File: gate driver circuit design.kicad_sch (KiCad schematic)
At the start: 22 parts, among them U1 SN6501QDBVRQ1, U2 SN6501QDBVRQ1

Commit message: Completed schematic design of gate driver
added components to schematic 27th May 2024
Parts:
- removed U2: SN6501QDBVRQ1, SOT95P280X145-5N, symbol SN6501QDBVRQ1:SN6501QDBVRQ1
- added C16, C18, C23, C26, C7: 4.7µF, symbol Device:C
- added C17, C19, C23, C24 (x2), C25, C27, C33, C37: 0.1µF, symbol Device:C
- added C20, C21, C25, C28: 0.01µF, symbol Device:C
- added C22, C35, C41, C42, C43: 100µF, symbol Device:C
- added C29: 100pF, symbol Device:C
- added C34: 27pF, symbol Device:C
- added C36: 470pF, symbol Device:C
- added C39, C40: 1000pF, symbol Device:C
- added D1, D2: BAV70-E3-08, SOT_70-E3-08_VIS, symbol 2024-05-25_06-21-47:BAV70-E3-08
- added D3, D4: MBRA340T3G, DIOM5226X220N, symbol MBRA340T3G:MBRA340T3G
- added D4, Q2, Q3: MMBT3904T-7-F, SOT50P160X90-3N, symbol MMBT3904T-7-F:MMBT3904T-7-F
- added D5, D7, D8: 1N4148X-TP, SODFL1608X70N, symbol 1N4148X-TP:1N4148X-TP
- added D6: BYG23T-M3/TR, DIOM5127X229N, symbol BYG23T-M3_TR:BYG23T-M3_TR
- added D9: 5.1V, SOD3716X135N, symbol BZT52C5V1-G3-08:BZT52C5V1-G3-08
- added IC1: LMV762QMA_NOPB, SOIC127P600X175-8N, symbol LMV762QMA_NOPB:LMV762QMA_NOPB
- added J101: 90122-0763, 90122-0763:MOLEX_90122-0763, symbol 90122-0763:90122-0763
- added J102, J103: 90121-0762, HDRRA2W64P0X254_1X2_508X250X360P, symbol 90121-0762:90121-0762
- added Q1: CSD17313Q2, CSD17313Q2:TRANS_CSD17313Q2, symbol CSD17313Q2:CSD17313Q2
- added R10, R7: 5.11, symbol Device:R
- added R11, R8: 1.0, symbol Device:R
- added R12, R14, R18, R28: 10.0k, symbol Device:R
- added R13, R22: 2.2k, symbol Device:R
- added R13: 27, symbol Device:R
- added R132, R27: 0, symbol Device:R
- added R15, R20, R23, R25, R26, R30: 5.1k, symbol Device:R
- added R16, R17, R19: 1.0k, symbol Device:R
- added R21: 1.00k, symbol Device:R
- added R24: 2k, symbol Device:R
- added R29: 15k, symbol Device:R
- added R8, R9 (x2): R, symbol Device:R
- added T1, T2: 750343725, PushPull_750343725:WE-PPTI_1209_L12.7W9.14H7.62, symbol PushPull_750343725:750343725
- added U2: TPS7B6950QDCYRQ1, TPS7B6950QDCYRQ1:VREG_TPS7B6950QDCYRQ1, symbol TPS7B6950QDCYRQ1:TPS7B6950QDCYRQ1
- added U3, U5, U9: TL431AQDBZRQ1, DBZ3, symbol TL431AQDBZRQ1:TL431AQDBZRQ1
- added U4: SN6501QDBVRQ1, SOT95P280X145-5N, symbol SN6501QDBVRQ1:SN6501QDBVRQ1
- added U6: UCC21530QDWKRQ1, UCC21530QDWKRQ1, symbol UCC21530QDWKRQ1:UCC21530QDWKRQ1
- added U7: ISO7721QDRQ1, SOIC127P600X175-8N, symbol ISO7721QDRQ1:ISO7721QDRQ1
- C15: value 0.1µF -> C
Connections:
- net 5Vin is gone; now on net GND: C10.1, C11.1, C2.1, C3.1, U1.2 (VCC)
- net +15Va: now also C19.1, C20.1, D1.3; no longer C12.2, C13.2, C14.2, C9.2, R4.1
- net -4Va: now also C16.1, C17.1, C21.1, T1.5, T2.5, U3.3 (ANODE), U5.3 (ANODE), U6.14 (VSSA); no longer C1.1, C15.2, C8.2, C9.1, R1.2, R2.1, R4.2, R5.1
- net GND: now also C22.1, C22.2, C35.1, D4.2 (E), J101.3, R132.2, R30.1, T1.2, T2.2, U4.2 (VCC), U4.4 (GND_1), U4.5 (GND_2), U6.3 (VCCI_1), U6.8 (VCCI_2), U7.1 (VCC1), U7.4 (GND1)
- net at R2.2, R3.1: now also U3.2 (REF)
- net at R5.2, R6.1: now also U5.2 (REF)
- net at U1.1 (D1): now also T1.3
- net at U1.3 (D2): now also T1.1
- new net: D2.1, T2.6
- new net: D2.2, T2.4
- new net: C41.2, R9.2, U6.2 (INB)
- new net: C41.1, C42.1, C43.1, R9.2, U6.4 (GND)
- new net: C43.2, R9.1, U6.6 (DT)
- new net: C42.2, R8.2, U6.1 (INA)
- new net: C24.2, D4.1 (K), R10.1, U6.10 (OUTB)
- new net: C23.2, D3.1 (K), R7.1, U6.15 (OUTA)
- new net: C18.1, U6.16 (VDDA)
- new net: D4.3 (C), R27.1, R30.2, U6.5 (EN)
- new net: IC1.3 (+IN_A), Q3.3 (C), R17.2, R21.1
- new net: C35.2, R23.2, U7.3 (INB)
- new net: C34.2, D8.1 (K), R21.2, R25.2
- new net: D7.2 (A), IC1.1 (OUT_A), R16.1, R22.2
- new net: Q2.1 (B), R16.2
- new net: D3.2 (A), R8.1
- new net: T2.3, U4.1 (D1)
- new net: T2.1, U4.3 (D2)
- new net: IC1.2 (-IN_A), IC1.6 (-IN_B), R20.1, R24.2, U9.1 (CATHODE)
- new net: IC1.5 (+IN_B), R22.1
- new net: IC1.7 (OUT_B), U7.7 (INA)
- new net: D7.1 (K), R17.1
- new net: Q1.3, Q2.2 (E), R19.1
- new net: D8.2 (A), D9.1 (K), R18.1, R26.2
- new net: D1.1, T1.6
- new net: D1.2, T1.4
- new net: Q1.1, Q1.2, Q1.5, Q1.6, Q1.8, R13.1
- new net: D5.2 (A), D6.2 (A), R15.1, R18.2
- new net: J101.4, R132.1
- new net: R24.1, R28.2, U9.2 (REF)
- new net: D4.2 (A), R11.1
- new net: C25.1, R13.2
- new net +15Vb: C12.2, C13.2, C14.2, C26.1, C27.1, C28.1, C9.2, D2.3, R4.1, U2.1 (IN), U6.11 (VDDB)
- new net -4Vb: C23.1, C24.1, C25.1, C29.1, C33.1, C34.1, C36.1, C37.1, C7.2, D9.2 (A), IC1.4 (V-), Q1.4, Q1.7, Q3.2 (E), R13.1, R19.2, R25.1, R26.1, R28.1, R29.1, U2.2 (GND_2), U2.4 (GND_4), U6.9 (VSSB), U7.5 (GND2), U7.6 (OUTB), U9.3 (ANODE)
- new net Coma: C1.1, C16.2, C17.2, C18.2, C19.2, C20.2, C21.2, C39.1, C8.2, D6.1 (K), J103.1, R1.2, R12.2, R2.1, U3.1 (CATHODE)
- new net Comb: C15.2, C23.2, C24.2, C25.2, C26.2, C27.2, C28.2, C40.1, C9.1, J102.1, R14.2, R4.2, R5.1, U5.1 (CATHODE)
- new net FLT: D4.1 (B), J101.2, R27.2, U7.2 (OUTA)
- new net G1: C23.1, C39.2, J103.2, R12.1, R7.2, R8.2
- new net G2: C24.1, C25.2, C40.2, D5.1 (K), J102.2, R10.2, R11.2, R14.1, R15.2
- new net RESET: J101.1, R23.1
- new net Vcc5V: C29.2, C33.2, C37.2, C7.1, IC1.8 (V+), Q2.3 (C), Q3.1 (B), R13.2, R20.2, R29.2, U2.3 (OUT), U7.8 (VCC2)
- new net Vg1: J101.6, R8.1
- new net Vg2: J101.5, R9.1
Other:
- note added: "750343725"
- note added: "Bottom Switch"
- note added: "Top Switch"
- moved on the sheet: C1, C2, C3, C4, C5, C6, C8, R1, R2, R3, U1

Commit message: Schematic Design Completed For Gate Driver
Schematic Design Completed For Gate Driver
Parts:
- removed C1, C11, C14, C17, C19, C23, C24 (x2), C25, C27, C3, C33, C37, C6, C9: 0.1µF, symbol Device:C
- removed C10, C2: 10µF, symbol Device:C
- removed C12, C13, C16, C18, C23, C26, C4, C5, C7: 4.7µF, symbol Device:C
- removed C15, C8: C, symbol Device:C
- removed C20, C21, C25, C28: 0.01µF, symbol Device:C
- removed C22, C35, C41, C42, C43: 100µF, symbol Device:C
- removed C29: 100pF, symbol Device:C
- removed C34: 27pF, symbol Device:C
- removed C36: 470pF, symbol Device:C
- removed C39, C40: 1000pF, symbol Device:C
- removed R1, R4: 4.7k, symbol Device:R
- removed R10, R7: 5.11, symbol Device:R
- removed R11, R8: 1.0, symbol Device:R
- removed R12, R14, R18, R28: 10.0k, symbol Device:R
- removed R13, R22: 2.2k, symbol Device:R
- removed R13: 27, symbol Device:R
- removed R132: 0, symbol Device:R
- removed R15, R20, R23, R25, R26, R30: 5.1k, symbol Device:R
- removed R16, R17, R19: 1.0k, symbol Device:R
- removed R2, R5: 3.01k, symbol Device:R
- removed R21: 1.00k, symbol Device:R
- removed R24: 2k, symbol Device:R
- removed R29: 15k, symbol Device:R
- removed R3, R6: 4.99k, symbol Device:R
- removed R8, R9 (x2): R, symbol Device:R
- added C1, C11, C14, C15, C17, C19, C22, C25, C27, C29, C3, C32, C33, C37, C6, C8, C9: 0.1µF, CAPC2012X90N, symbol 0805B104K250CT:0805B104K250CT
- added C10, C2: 10µF, CAPC2012X135N, symbol LMK212ABJ106KGHT:LMK212ABJ106KGHT
- added C12, C13, C16, C18, C26, C28, C4, C5, C7: 4.7µF, GRT21BR61E226ME13L, symbol GRT21BR61H475KE13L:GRT21BR61H475KE13L
- added C20, C21, C30, C31: 0.01µF, CAPC2012X95N, symbol GRM2195C1H103JA01D:GRM2195C1H103JA01D
- added C23, C24: 0.1µF, CAPC2012X95N, symbol AC0805KRX7R8BB104:AC0805KRX7R8BB104
- added C34: 27pF, CAPC2012X70N, symbol CC0805JRNPO9BN270:CC0805JRNPO9BN270
- added C35: 100µF, CAPC2012X75N, symbol CL21C101JBANNNC:CL21C101JBANNNC
- added C36: 470pF, C0805, symbol C0805C471J5GACTU:C0805C471J5GACTU
- added C38, C41, C42, C43: 100pF, C0805, symbol C0805C101J1GACAUTO:C0805C101J1GACAUTO
- added C39, C40: 1000pF, C0805, symbol C0805C102K5RACAUTO:C0805C102K5RACAUTO
- added R1, R4: 4.7k, RESC2012X50N, symbol CRCW08054K70JNEA:CRCW08054K70JNEA
- added R10, R7: 5.11, RESC3216X60N, symbol CRCW12065R11FKEA:CRCW12065R11FKEA
- added R11, R8: 1.0, RESC3116X65N, symbol CRM1206-JW-1R0ELF:CRM1206-JW-1R0ELF
- added R12, R14, R18, R28: 10.0k, RESC2012X60N, symbol RC0805JR-131KL:RC0805JR-131KL
- added R13: 27, RESC3216X60N, symbol CRCW120627R0JNEA:CRCW120627R0JNEA
- added R132, R33, R34: 0, ERJS06_U06_(0805), symbol ERJ-U060R00V:ERJ-U060R00V
- added R15, R20, R23, R25, R26, R30, R32: 5.1k, RESC2012X60N, symbol CR0805-FX-5101ELF:CR0805-FX-5101ELF
- added R16, R17, R19, R27: 1.0k, RESC2012X60N, symbol RC0805JR-131KL:RC0805JR-131KL
- added R2, R5: 3.01k, RESC2012X60N, symbol RC0805JR-131KL:RC0805JR-131KL
- added R21: 1.00k, RESC2012X60N, symbol RC0805JR-131KL:RC0805JR-131KL
- added R22: 2.2k, RESC2012X60N, symbol RC0805JR-131KL:RC0805JR-131KL
- added R24: 2.00k, RESC2012X60N, symbol RC0805JR-131KL:RC0805JR-131KL
- added R29: 15k, RESC2012X50N, symbol CRCW080515K0JNEA:CRCW080515K0JNEA
- added R3, R6: 4.99k, RESC2013X65N, symbol RR1220P-4991-D-M:RR1220P-4991-D-M
- added R9: 1k, RESC2012X60N, symbol RC0805JR-131KL:RC0805JR-131KL
- renumbered D4 to Q4, R27 to R31, IC1 to U8
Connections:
- net +15Va: now also C1.2, C19.1, C20.1, C4.2, C5.2, C6.2, R1.2
- net +15Vb: now also C12.2, C13.2, C14.2, C28.2, C29.2, C31.2, C9.2, R4.2
- net -4Va: now also C16.1, C17.1, C21.1, C4.1, C5.1, C6.1, C8.1, R3.1 (R1); no longer T2.5, U5.3 (ANODE)
- net -4Vb: now also T2.5, U5.3 (ANODE), C12.1, C13.1, C14.1, C15.1, C26.2, C27.2, C30.2, C33.1, C34.1, C36.1, C36.2, C37.1, C38.1, C7.1, R19.2, R25.1, R26.1, R27.1, R28.1, R29.1, R6.1 (R1)
- net Coma: now also C1.1, C16.2, C17.2, C18.2, C19.2, C20.2, C21.2, C39.2, C8.2, R1.1, R12.1, R2.2
- net Comb: now also C15.2, C26.1, C27.1, C28.1, C29.1, C30.1, C31.1, C40.2, C9.1, R14.1, R4.1, R5.2
- net FLT: now also R32.2; no longer Q4.1 (B)
- net G1: now also C23.2, C39.1, R12.2, R7.2, R8.2
- net G2: now also C24.2, C25.2, C40.1, R10.2, R11.2, R14.2, R15.2
- net GND: now also C10.2, C11.1, C2.2, C22.1, C3.1, C32.1, C35.1; no longer T1.2, T2.2, U1.2 (VCC), U4.2 (VCC), U6.3 (VCCI_1), U6.8 (VCCI_2), U7.1 (VCC1)
- net RESET: now also R23.2
- net Vcc5V: now also C33.2, C37.2, C38.2, C7.2, R20.2, R27.2, R29.2
- net Vg1: now also R33.1
- net Vg2: now also R34.1
- net at U6.2 (INB): now also C41.2, R34.2
- net at U6.4 (GND): now also C41.1, C42.1, C43.1, R9.1
- net at U6.6 (DT): now also C43.2, R9.2
- net at U6.1 (INA): now also C42.2, R33.2
- net at D4.1 (K), U6.10 (OUTB): now also C24.1, R10.1
- net at D3.1 (K), U6.15 (OUTA): now also C23.1, R7.1
- net at U6.16 (VDDA): now also C18.1
- net at Q4.3 (C), R31.1, U6.5 (EN): now also R30.1
- net at Q3.3 (C), U8.3 (+IN_A): now also R17.2, R21.2
- net at U7.3 (INB): now also C35.2, R23.1
- net at U3.2 (REF): now also R2.1, R3.2 (R2)
- net at U5.2 (REF): now also R5.1, R6.2 (R2)
- net at D8.1 (K): now also C34.2, R21.1, R25.2
- net at D7.2 (A), U8.1 (OUT_A): now also R16.1, R22.1
- net at Q2.1 (B): now also R16.2
- net at D3.2 (A): now also R8.1
- net at U8.2 (-IN_A), U8.6 (-IN_B), U9.1 (CATHODE): now also R20.1, R24.2
- net at U8.5 (+IN_B): now also R22.2
- net at D7.1 (K): now also R17.1
- net at Q1.3, Q2.2 (E): now also R19.1
- net at D8.2 (A), D9.1 (K): now also R18.1, R26.2
- net at Q1.1, Q1.2, Q1.5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: now also R13.1
- net at D5.2 (A), D6.2 (A): now also R15.1, R18.2
- net at J101.4: now also R132.1
- net at U9.2 (REF): now also R24.1, R28.2
- net at D4.2 (A): now also R11.1
- new net: C25.1, R13.2
- new net: Q4.1 (B), R32.1
- new net 5Vin: C10.1, C11.2, C2.1, C22.2, C3.2, C32.2, R132.2, R30.2, T1.2, T2.2, U1.2 (VCC), U4.2 (VCC), U6.3 (VCCI_1), U6.8 (VCCI_2), U7.1 (VCC1)
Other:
- note added: "DAKSH PAWAR"
- note added: "Gate Driver"
- note added: "Header"
- note added: "Low-Dropout Regulator"
- note added: "Push Pull Transformer"
- title: (none) -> Gate Driver Circuit Design
- moved on the sheet: D1, D2, D3, D4, D5, D6, D7, D8, D9, J101, J102, J103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

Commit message: SCHEMATIC FINAL
FINAL DESIGN OF SCHEMATIC
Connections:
- net +15Va: now also C18.1, U6.16 (VDDA)
- net -4Vb: no longer C36.2, R27.1, U7.6 (OUTB)
- net GND: now also C41.1, C42.1, C43.1, R9.1, U6.4 (GND)
- net Vcc5V: no longer C38.2, Q3.1 (B), R27.2, R29.2
- net at R22.2, U8.5 (+IN_B): now also C36.2
- new net: R27.1, U7.6 (OUTB)
- new net: C38.2, Q3.1 (B), R27.2, R29.2
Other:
- note added: "GATE DRIVER CIRCUIT DESIGN TIDA-01605 DAKSH PAWAR"
- note removed: "DAKSH PAWAR"
- title: Gate Driver Circuit Design -> Gate Driver Circuit Design TIDA-01605
- moved on the sheet: C15, C36, C8, R26

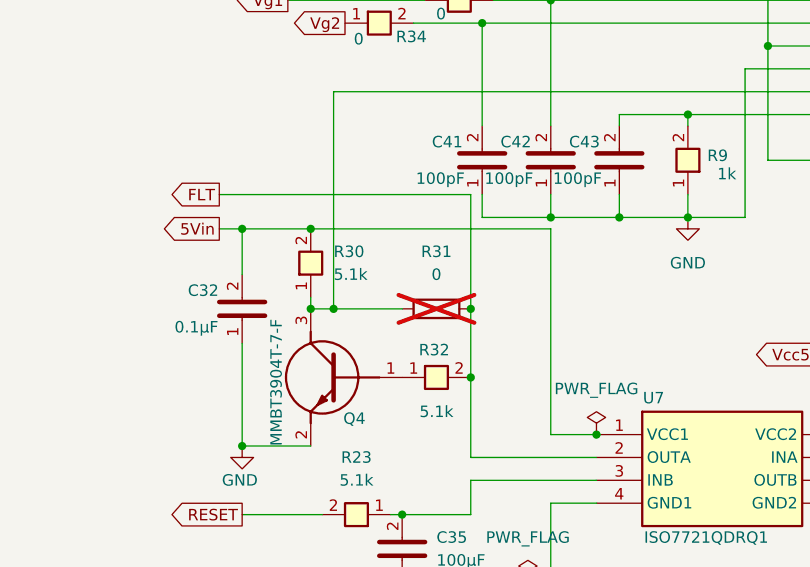
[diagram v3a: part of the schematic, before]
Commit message: PLACED COMPONENTS ON PCB AND DESIGNED 3D MODEL OF PCB
PLACED COMPONENTS ON PCB AND DESIGNED 3D MODEL OF PCB
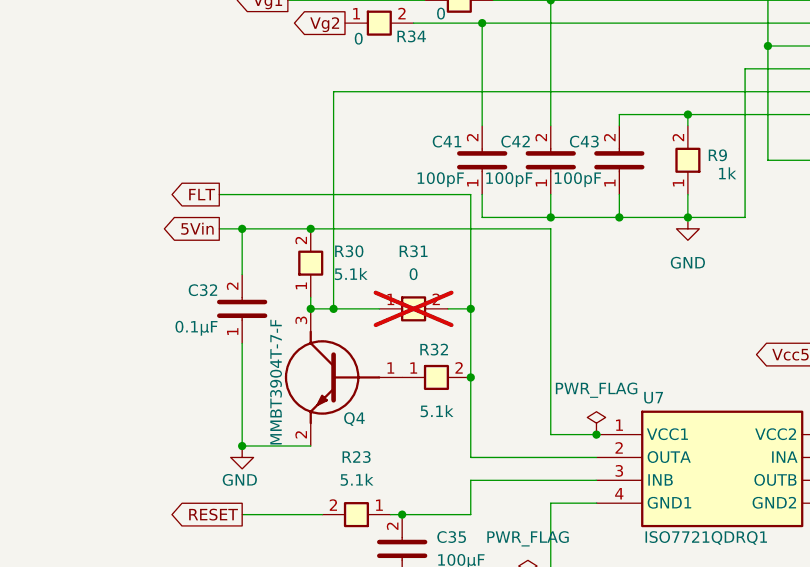
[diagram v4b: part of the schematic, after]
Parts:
- removed R31: 0, symbol Device:R
- added R31: 0, ERJ-U060R00V:ERJS06_U06__0805_, symbol ERJ-U060R00:ERJ-U060R00V
- R132, R33, R34: footprint ERJS06_U06_(0805) -> ERJ-U060R00V:ERJS06_U06__0805_
- T1, T2: footprint PushPull_750343725:WE-PPTI_1209_L12.7W9.14H7.62 -> 750343725:TRANSFORMER_750343725_WRE-L
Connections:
- net FLT: now also R31.2
- net at Q4.3 (C), R30.1, U6.5 (EN): now also R31.1
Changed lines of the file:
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@@
 	(wire
 		(pts
+			(xy 106.68 168.91) (xy 109.22 168.91)
+		)
+		(stroke
+			(width 0)
+			(type default)
+		)
+	)
+	(wire
+		(pts
 			(xy 181.61 134.62) (xy 181.61 128.27)
 		)
@@
 	(wire
 		(pts
-			(xy 93.98 168.91) (xy 101.6 168.91)
+			(xy 93.98 168.91) (xy 99.06 168.91)
 		)
 		(stroke
@@
 	)
 	(symbol
+		(lib_id "ERJ-U060R00:ERJ-U060R00V")
+		(at 96.52 168.91 0)
+		(unit 1)
+		(exclude_from_sim no)
+		(in_bom yes)
+		(on_board yes)
+		(dnp yes)
+		(fields_autoplaced yes)
+		(property "Reference" "R31"
+			(at 102.87 162.56 0)
+			(effects
+				(font
+					(size 1.27 1.27)
+				)
+			)
+		)
+		(property "Value" "0"
+			(at 102.87 165.1 0)
+			(effects
+				(font
+					(size 1.27 1.27)
+				)
+			)
+		)
+		(property "Footprint" "ERJ-U060R00V:ERJS06_U06__0805_"
+			(at 110.49 265.1 0)
+			(effects
+				(font
+					(size 1.27 1.27)
+				)
+				(justify left top)
+				(hide yes)
+			)
+		)
+		(property "Datasheet" "https://industrial.panasonic.com/cdbs/www-data/pdf/RDP0000/AOA0000C334.pdf"
+			(at 110.49 365.1 0)
+			(effects
+				(font
+					(size 1.27 1.27)
+				)
+				(justify left top)
+				(hide yes)
+			)
+		)
+		(property "Description" "Anti-Sulfurated Thick Film Chip Resistor, 0805, 0.125W"
+			(at 100.584 158.496 0)
+			(effects
+				(font
+					(size 1.27 1.27)
+				)
+				(hide yes)
+			)
+		)
+		(property "Height" "0.7"
+			(at 110.49 565.1 0)
+			(effects
+				(font
+					(size 1.27 1.27)
+				)
+				(justify left top)
+				(hide yes)
+			)
+		)
+		(property "Mouser Part Number" "667-ERJ-U060R00V"
+			(at 110.49 665.1 0)
+			(effects
+				(font
+					(size 1.27 1.27)
+				)
+				(justify left top)
+				(hide yes)
+			)
+		)
+		(property "Mouser Price/Stock" "https://www.mouser.co.uk/ProductDetail/Panasonic/ERJ-U060R00V?qs=tfZGHB2PWd2kedEYcf1%2FXQ%3D%3D"
+			(at 110.49 765.1 0)
+			(effects
+				(font
+					(size 1.27 1.27)
+				)
+				(justify left top)
+				(hide yes)
+			)
+		)
+		(property "Manufacturer_Name" "Panasonic"
+			(at 110.49 865.1 0)
+			(effects
+				(font
+					(size 1.27 1.27)
+				)
+				(justify left top)
+				(hide yes)
+			)
+		)
+		(property "Manufacturer_Part_Number" "ERJ-U060R00V"
+			(at 110.49 965.1 0)
+			(effects
+				(font
+					(size 1.27 1.27)
+				)
+				(justify left top)
+				(hide yes)
+			)
+		)
+		(pin "2"
+		)
+		(pin "1"
+		)
+		(instances
+			(project "gate driver circuit design"
+				(path "/b1aff707-7082-456c-8309-ea9a24dd8210"
+					(reference "R31")
+					(unit 1)
+				)
+			)
+		)
+	)
+	(symbol
 		(lib_name "C0805C101J1GACAUTO_1")
 		(lib_id "C0805C101J1GACAUTO:C0805C101J1GACAUTO")
@@
 			)
 		)
-		(property "Footprint" "PushPull_750343725:WE-PPTI_1209_L12.7W9.14H7.62"
+		(property "Footprint" "750343725:TRANSFORMER_750343725_WRE-L"
 			(at 107.95 30.48 0)
 			(effects
@@
 			)
 		)
-		(property "Footprint" "ERJS06_U06_(0805)"
+		(property "Footprint" "ERJ-U060R00V:ERJS06_U06__0805_"
 			(at 314.96 181.28 0)
 			(effects
@@
 	)
 	(symbol
-		(lib_id "Device:R")
-		(at 105.41 168.91 90)
-		(unit 1)
-		(exclude_from_sim no)
-		(in_bom yes)
-		(on_board yes)
-		(dnp yes)
-		(fields_autoplaced yes)
-		(property "Reference" "R31"
-			(at 105.41 162.56 90)
-			(effects
-				(font
-					(size 1.27 1.27)
-				)
-			)
-		)
-		(property "Value" "0"
-			(at 105.41 165.1 90)
-			(effects
-				(font
-					(size 1.27 1.27)
-				)
-			)
-		)
-		(property "Footprint" ""
-			(at 105.41 170.688 90)
-			(effects
-				(font
-					(size 1.27 1.27)
-				)
-				(hide yes)
-			)
-		)
-		(property "Datasheet" "~"
-			(at 105.41 168.91 0)
-			(effects
-				(font
-					(size 1.27 1.27)
-				)
-				(hide yes)
-			)
-		)
-		(property "Description" "Resistor"
-			(at 105.41 168.91 0)
-			(effects
-				(font
-					(size 1.27 1.27)
-				)
-				(hide yes)
-			)
-		)
-		(pin "1"
-		)
-		(pin "2"
-		)
-		(instances
-			(project "gate driver circuit design"
-				(path "/b1aff707-7082-456c-8309-ea9a24dd8210"
-					(reference "R31")
-					(unit 1)
-				)
-			)
-		)
-	)
-	(symbol
 		(lib_name "GRT21BR61H475KE13L_1")
 		(lib_id "GRT21BR61H475KE13L:GRT21BR61H475KE13L")
@@
 			)
 		)
-		(property "Footprint" "PushPull_750343725:WE-PPTI_1209_L12.7W9.14H7.62"
+		(property "Footprint" "750343725:TRANSFORMER_750343725_WRE-L"
 			(at 107.95 62.23 0)
 			(effects
@@
 			)
 		)
-		(property "Footprint" "ERJS06_U06_(0805)"
+		(property "Footprint" "ERJ-U060R00V:ERJS06_U06__0805_"
 			(at 101.6 233.35 0)
 			(effects
@@
 			)
 		)
-		(property "Footprint" "ERJS06_U06_(0805)"
+		(property "Footprint" "ERJ-U060R00V:ERJS06_U06__0805_"
 			(at 110.49 230.81 0)
 			(effects

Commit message: PCB Routing Last Stage
PCB Routing Last Stage
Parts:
- R33: footprint ERJ-U060R00V:ERJS06_U06__0805_ -> CR0805-FX-5101ELF:RESC2012X60N
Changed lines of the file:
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@@
 			)
 		)
-		(property "Footprint" "ERJ-U060R00V:ERJS06_U06__0805_"
+		(property "Footprint" "CR0805-FX-5101ELF:RESC2012X60N"
 			(at 110.49 230.81 0)
 			(effects
